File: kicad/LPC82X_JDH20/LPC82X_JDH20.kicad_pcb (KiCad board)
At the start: 2 copper layers, 18.7 x 23.8 mm, 24 parts, among them J1 Conn_01x09, J2 JTAG_2X05, J3 Conn_01x09, U1 LPC824M201JDH20, Y1 12MHz

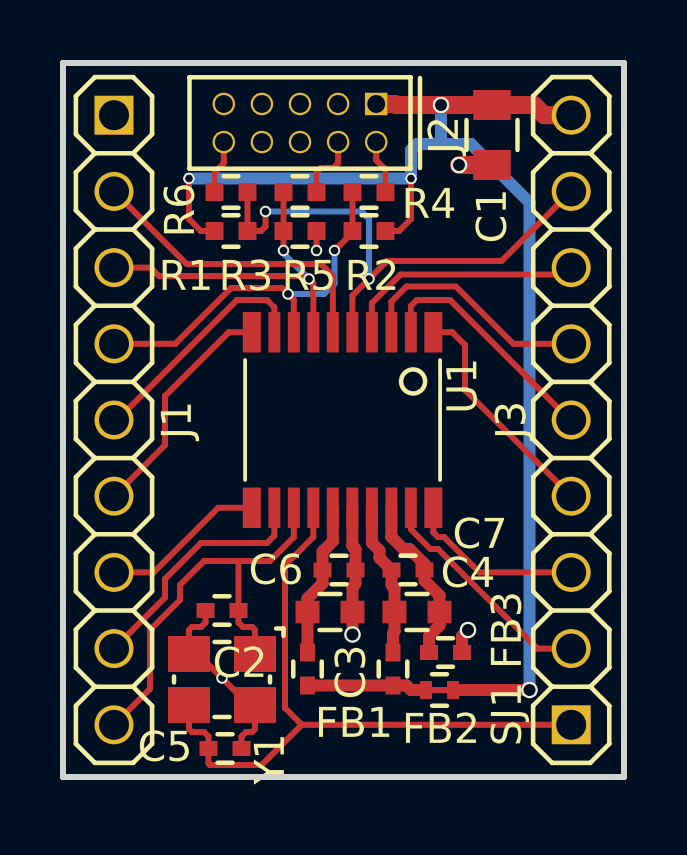
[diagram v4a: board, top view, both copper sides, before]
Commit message: small trace change, updated version number
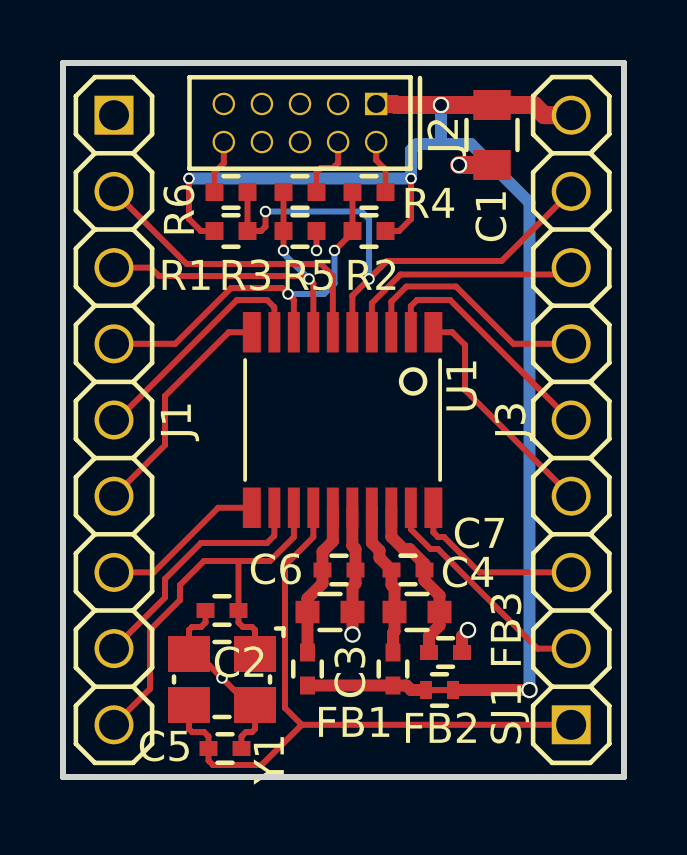
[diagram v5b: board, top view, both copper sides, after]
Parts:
- N2: value 20181110 -> 20190119
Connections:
- J2 pad 6: (no net) -> Net-(J2-Pad6)
- J2 pad 7: (no net) -> Net-(J2-Pad7)
- J2 pad 8: (no net) -> Net-(J2-Pad8)
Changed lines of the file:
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@@
     (zones 0)
     (modules 24)
-    (nets 26)
+    (nets 29)
   )
   (page A4)
@@
   (net 24 /PIO0_14)
   (net 25 /PIO0_0)
+  (net 26 "Net-(J2-Pad6)")
+  (net 27 "Net-(J2-Pad7)")
+  (net 28 "Net-(J2-Pad8)")
   (net_class Default "This is the default net class."
     (clearance 0.1524)
@@
     (add_net "Net-(J2-Pad2)")
     (add_net "Net-(J2-Pad4)")
+    (add_net "Net-(J2-Pad6)")
+    (add_net "Net-(J2-Pad7)")
+    (add_net "Net-(J2-Pad8)")
     (add_net VDD)
     (add_net VSS)
@@
       (effects (font (size 1 1) (thickness 0.15)) (justify mirror))
     )
-    (fp_text value 20181110 (at -0.4 0.1) (layer B.SilkS)
+    (fp_text value 20190119 (at -0.4 0.1) (layer B.SilkS)
       (effects (font (size 1 1) (thickness 0.15)) (justify mirror))
     )
@@
     (pad 5 thru_hole circle (at 0 0.635 180) (size 0.75 0.75) (drill 0.6) (layers *.Cu *.Mask)
       (net 1 VSS))
-    (pad 6 thru_hole circle (at 0 -0.635 180) (size 0.75 0.75) (drill 0.6) (layers *.Cu *.Mask))
-    (pad 7 thru_hole circle (at 1.27 0.635 180) (size 0.75 0.75) (drill 0.6) (layers *.Cu *.Mask))
-    (pad 8 thru_hole circle (at 1.27 -0.635 180) (size 0.75 0.75) (drill 0.6) (layers *.Cu *.Mask))
+    (pad 6 thru_hole circle (at 0 -0.635 180) (size 0.75 0.75) (drill 0.6) (layers *.Cu *.Mask)
+      (net 26 "Net-(J2-Pad6)"))
+    (pad 7 thru_hole circle (at 1.27 0.635 180) (size 0.75 0.75) (drill 0.6) (layers *.Cu *.Mask)
+      (net 27 "Net-(J2-Pad7)"))
+    (pad 8 thru_hole circle (at 1.27 -0.635 180) (size 0.75 0.75) (drill 0.6) (layers *.Cu *.Mask)
+      (net 28 "Net-(J2-Pad8)"))
     (pad 9 thru_hole circle (at 2.54 0.635 180) (size 0.75 0.75) (drill 0.6) (layers *.Cu *.Mask)
       (net 1 VSS))
@@
   (segment (start 130.15 112.15) (end 130.15 112.55) (width 0.2) (layer F.Cu) (net 7))
   (segment (start 130 112) (end 130.15 112.15) (width 0.2) (layer F.Cu) (net 7))
-  (segment (start 130.15 112.55) (end 130.15 113.05) (width 0.2) (layer F.Cu) (net 7))
-  (segment (start 130.15 113.05) (end 130.2 113.1) (width 0.2) (layer F.Cu) (net 7))
   (segment (start 131.92 113.1) (end 133.26 111.76) (width 0.2) (layer F.Cu) (net 7))
-  (segment (start 130.2 113.1) (end 131.92 113.1) (width 0.2) (layer F.Cu) (net 7))
+  (segment (start 131.92 113.1) (end 130.3 113.1) (width 0.2) (layer F.Cu) (net 7))
+  (segment (start 130.15 112.95) (end 130.15 112.55) (width 0.2) (layer F.Cu) (net 7))
+  (segment (start 130.3 113.1) (end 130.15 112.95) (width 0.2) (layer F.Cu) (net 7))
   (segment (start 133.45 110.45) (end 136.3 110.45) (width 0.4) (layer F.Cu) (net 8))
   (segment (start 136.3 110.45) (end 136.75 110.45) (width 0.4) (layer F.Cu) (net 8))

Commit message: fixed mistake in microcontroller power, updated library component, added newer component library, rerouted
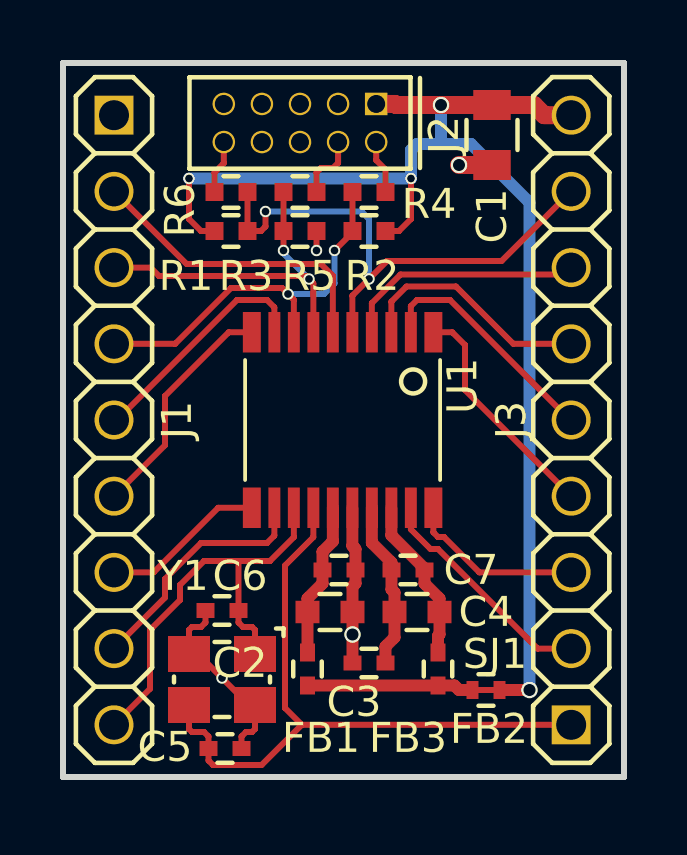
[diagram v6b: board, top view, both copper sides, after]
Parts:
- moved FB3 2.57 mm to (135.5, 109.7), turned to 180 degrees
- moved SJ1 1.55 mm to (139.4, 110.6)
- moved FB2 1.50 mm to (137.8, 109.9)
- turned C4 to 180 degrees
- turned C7 to 180 degrees
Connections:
- J2 pad 6: Net-(J2-Pad6) -> (no net)
- J2 pad 7: Net-(J2-Pad7) -> (no net)
- J2 pad 8: Net-(J2-Pad8) -> (no net)
- U1 pad 17: Net-(C4-Pad1) -> Net-(C4-Pad2)
- U1 pad 18: Net-(C4-Pad2) -> Net-(C4-Pad1)
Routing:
- net VDD: track 44.7 -> 43.1 mm
- net Net-(FB1-Pad2): track 4.01 -> 5.56 mm
- net VSS: track 13.4 -> 13.5 mm, vias 5 -> 4

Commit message: updated silkscreen
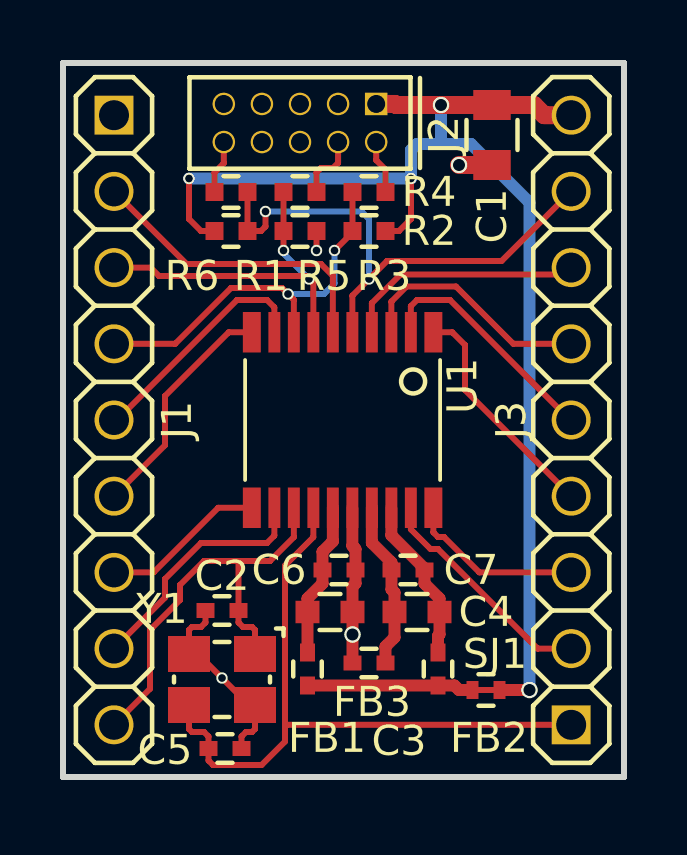
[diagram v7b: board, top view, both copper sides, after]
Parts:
- N2: value 20190119 -> 20190121
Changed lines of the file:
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@@
   )
   (setup
-    (last_trace_width 0.4)
+    (last_trace_width 0.2)
     (user_trace_width 0.1524)
     (user_trace_width 0.2)
@@
     (at 130.6 110.25 180)
     (attr smd)
-    (fp_text reference Y1 (at 1.3 3.45 180) (layer F.SilkS)
+    (fp_text reference Y1 (at 2 2.35 180) (layer F.SilkS)
       (effects (font (size 1 1) (thickness 0.15)))
     )
@@
       (effects (font (size 1 1) (thickness 0.15)) (justify mirror))
     )
-    (fp_text value 20190119 (at -0.4 0.1) (layer B.SilkS)
+    (fp_text value 20190121 (at -0.4 0.1) (layer B.SilkS)
       (effects (font (size 1 1) (thickness 0.15)) (justify mirror))
     )
@@
     (tags "capacitor 0402")
     (attr smd)
-    (fp_text reference C2 (at -0.6 -1.75) (layer F.SilkS)
+    (fp_text reference C2 (at 0 1.15) (layer F.SilkS)
       (effects (font (size 1 1) (thickness 0.15)))
     )
@@
     (tags "capacitor 0603")
     (attr smd)
-    (fp_text reference C3 (at 0.8 3) (layer F.SilkS)
+    (fp_text reference C3 (at 2.3 4.3) (layer F.SilkS)
       (effects (font (size 1 1) (thickness 0.15)))
     )
@@
     (tags "capacitor 0402")
     (attr smd)
-    (fp_text reference C5 (at -2 -0.05) (layer F.SilkS)
+    (fp_text reference C5 (at -2 0.05) (layer F.SilkS)
       (effects (font (size 1 1) (thickness 0.15)))
     )
@@
     (tags "capacitor 0402")
     (attr smd)
-    (fp_text reference C6 (at -3.3 0.2) (layer F.SilkS)
+    (fp_text reference C6 (at -2 0) (layer F.SilkS)
       (effects (font (size 1 1) (thickness 0.15)))
     )
@@
     (tags "capacitor 0402")
     (attr smd)
-    (fp_text reference FB1 (at 2.3 -0.45 180) (layer F.SilkS)
+    (fp_text reference FB1 (at 2.3 -0.65 180) (layer F.SilkS)
       (effects (font (size 1 1) (thickness 0.15)))
     )
@@
     (tags "capacitor 0402")
     (attr smd)
-    (fp_text reference FB2 (at 2 -1.7 180) (layer F.SilkS)
-      (effects (font (size 1 1) (thickness 0.15)))
-    )
-    (fp_text value FB (at 2 -1.6 180) (layer F.Fab)
+    (fp_text reference FB2 (at 2.3 -1.7 180) (layer F.SilkS)
+      (effects (font (size 1 1) (thickness 0.15)))
+    )
+    (fp_text value FB (at 2.3 -1.7 180) (layer F.Fab)
       (effects (font (size 1 1) (thickness 0.15)))
     )
@@
     (tags "capacitor 0402")
     (attr smd)
-    (fp_text reference FB3 (at -1.3 -2.5) (layer F.SilkS)
-      (effects (font (size 1 1) (thickness 0.15)))
-    )
-    (fp_text value FB (at -0.8 -2.5 180) (layer F.Fab)
+    (fp_text reference FB3 (at -0.1 -1.3) (layer F.SilkS)
+      (effects (font (size 1 1) (thickness 0.15)))
+    )
+    (fp_text value FB (at 0 -1.3 180) (layer F.Fab)
       (effects (font (size 1 1) (thickness 0.15)))
     )
@@
     (tags "resistor 0402")
     (attr smd)
-    (fp_text reference R1 (at -1.5 1.5) (layer F.SilkS)
-      (effects (font (size 1 1) (thickness 0.15)))
-    )
-    (fp_text value 100K (at -1.6 1.5) (layer F.Fab)
+    (fp_text reference R1 (at 1 1.5) (layer F.SilkS)
+      (effects (font (size 1 1) (thickness 0.15)))
+    )
+    (fp_text value 100K (at -0.2 1.5) (layer F.Fab)
       (effects (font (size 1 1) (thickness 0.15)))
     )
@@
     (tags "resistor 0402")
     (attr smd)
-    (fp_text reference R2 (at -0.1 -1.5 180) (layer F.SilkS)
-      (effects (font (size 1 1) (thickness 0.15)))
-    )
-    (fp_text value 100k (at -0.6 -1.6 180) (layer F.Fab)
+    (fp_text reference R2 (at -2 0 180) (layer F.SilkS)
+      (effects (font (size 1 1) (thickness 0.15)))
+    )
+    (fp_text value 100k (at -2.9 0 180) (layer F.Fab)
       (effects (font (size 1 1) (thickness 0.15)))
     )
@@
     (tags "resistor 0402")
     (attr smd)
-    (fp_text reference R3 (at 1.8 -1.5 180) (layer F.SilkS)
-      (effects (font (size 1 1) (thickness 0.15)))
-    )
-    (fp_text value 100k (at 1.6 -1.5 180) (layer F.Fab)
+    (fp_text reference R3 (at -2.8 -1.5 180) (layer F.SilkS)
+      (effects (font (size 1 1) (thickness 0.15)))
+    )
+    (fp_text value 100k (at -2.1 -1.5 180) (layer F.Fab)
       (effects (font (size 1 1) (thickness 0.15)))
     )
@@
     (tags "resistor 0402")
     (attr smd)
-    (fp_text reference R4 (at -2 -0.4 180) (layer F.SilkS)
+    (fp_text reference R4 (at -2 0 180) (layer F.SilkS)
       (effects (font (size 1 1) (thickness 0.15)))
     )
@@
     (tags "resistor 0402")
     (attr smd)
-    (fp_text reference R5 (at -0.3 -2.8 180) (layer F.SilkS)
+    (fp_text reference R5 (at -0.8 -2.8 180) (layer F.SilkS)
       (effects (font (size 1 1) (thickness 0.15)))
     )
@@
     (tags "resistor 0402")
     (attr smd)
-    (fp_text reference R6 (at -1.7 0.6 90) (layer F.SilkS)
-      (effects (font (size 1 1) (thickness 0.15)))
-    )
-    (fp_text value 100 (at -1.7 0.6 90) (layer F.Fab)
+    (fp_text reference R6 (at -1.3 2.8 180) (layer F.SilkS)
+      (effects (font (size 1 1) (thickness 0.15)))
+    )
+    (fp_text value 100 (at -1.2 2.8 180) (layer F.Fab)
       (effects (font (size 1 1) (thickness 0.15)))
     )
@@
   (segment (start 136.245 105.445) (end 136.245 104.525) (width 0.4) (layer F.Cu) (net 6))
   (segment (start 137.35 106.55) (end 136.245 105.445) (width 0.4) (layer F.Cu) (net 6))
-  (segment (start 133.645 104.525) (end 133.645 105.505) (width 0.2) (layer F.Cu) (net 7))
-  (segment (start 133.645 105.505) (end 132.7 106.45) (width 0.2) (layer F.Cu) (net 7))
-  (segment (start 132.7 106.45) (end 132.7 111.15) (width 0.2) (layer F.Cu) (net 7))
-  (segment (start 132.7 111.2) (end 132.7 111.15) (width 0.2) (layer F.Cu) (net 7))
-  (segment (start 142.24 111.76) (end 133.26 111.76) (width 0.2) (layer F.Cu) (net 7))
-  (segment (start 133.26 111.76) (end 132.7 111.2) (width 0.2) (layer F.Cu) (net 7))
   (segment (start 129.5 111.1) (end 129.5 111.9) (width 0.2) (layer F.Cu) (net 7))
   (segment (start 129.5 111.9) (end 129.6 112) (width 0.2) (layer F.Cu) (net 7))
@@
   (segment (start 130.15 112.15) (end 130.15 112.55) (width 0.2) (layer F.Cu) (net 7))
   (segment (start 130 112) (end 130.15 112.15) (width 0.2) (layer F.Cu) (net 7))
-  (segment (start 131.92 113.1) (end 133.26 111.76) (width 0.2) (layer F.Cu) (net 7))
+  (segment (start 130.15 112.95) (end 130.15 112.55) (width 0.2) (layer F.Cu) (net 7))
+  (segment (start 133.645 105.505) (end 132.7 106.45) (width 0.2) (layer F.Cu) (net 7))
+  (segment (start 132.7 112.32) (end 131.92 113.1) (width 0.2) (layer F.Cu) (net 7))
   (segment (start 131.92 113.1) (end 130.3 113.1) (width 0.2) (layer F.Cu) (net 7))
-  (segment (start 130.15 112.95) (end 130.15 112.55) (width 0.2) (layer F.Cu) (net 7))
+  (segment (start 133.645 104.525) (end 133.645 105.505) (width 0.2) (layer F.Cu) (net 7))
   (segment (start 130.3 113.1) (end 130.15 112.95) (width 0.2) (layer F.Cu) (net 7))
+  (segment (start 132.76 111.76) (end 132.7 111.7) (width 0.2) (layer F.Cu) (net 7))
+  (segment (start 142.24 111.76) (end 132.76 111.76) (width 0.2) (layer F.Cu) (net 7))
+  (segment (start 132.7 106.45) (end 132.7 111.7) (width 0.2) (layer F.Cu) (net 7))
+  (segment (start 132.7 111.7) (end 132.7 112.32) (width 0.2) (layer F.Cu) (net 7))
   (segment (start 138.95 110.6) (end 138.5 110.6) (width 0.4) (layer F.Cu) (net 8))
   (segment (start 138.35 110.45) (end 137.8 110.45) (width 0.4) (layer F.Cu) (net 8))
